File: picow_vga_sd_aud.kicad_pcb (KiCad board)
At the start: 2 copper layers, 74.4 x 53.1 mm, 98 parts, among them J1 10103594-0001LF, J10 Micro_SD_Card, J2 AudioJack3, J3 Micro_SD_Card, J4 L77HDE15SD1CH4F, J5 TSW-102-07-G-S, J6 Conn_01x18_Pin, J7 Conn_02x03_Odd_Even, SW1 SW_Push, SW2 SW_Push, SW3 SW_Push, SW4 SW_Push, SW5 SW_boot, U1 TLV70033_SOT23-5, U10 ER_OLEDM0.91_1x-I2C, U2 PicoW, U3 NC7WZ16P6X, U4 NCP1117ST33T3G, U5 W25Q128JVSIQ, U6 RP2040, U7 W25Q128JVSIQ, U8 TXS0108, U9 TXS0108, X1 12MHz

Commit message: Cambiar vias default de 0.8mm a 0.6mm de diámetro
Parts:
- moved R6 2.07 mm to (126.9, 63.1), turned to 0 degrees
- moved C25 0.15 mm to (124.8, 70.0)
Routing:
- net GND: track 515.5 -> 0.00 mm, vias 2 -> 0
- net /pico/QSPI_SS: track 145.6 -> 4.46 mm, vias 6 -> 0
- net /GPIO14: track 8.30 -> 23.7 mm
- net /GPIO13: track 21.2 -> 18.4 mm
- net +3V3: track 409.3 -> 411.6 mm
- net /GPIO12: track 24.8 -> 25.5 mm
- net /GPIO1: track 71.9 -> 72.5 mm

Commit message: Actualizar net classes y clearances del PCB
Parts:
- moved R6 20.3 mm to (128.8, 83.3), turned to 180 degrees
- moved C18 6.58 mm to (128.5, 82.3)
- moved C25 0.48 mm to (124.3, 70.0)
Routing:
- net /pico/QSPI_SD2: track 140.5 -> 0.00 mm, vias 6 -> 0
- net /GPIO14: track 23.7 -> 40.1 mm
- net /pico/QSPI_SS: track 4.46 -> 20.6 mm
- net /GPIO4: track 59.4 -> 46.6 mm, vias 3 -> 1
- net /GPIO3: track 38.8 -> 51.1 mm, vias 0 -> 1
- net /GPIO5: track 116.5 -> 110.9 mm
- net /GPIO1: track 72.5 -> 68.9 mm, vias 3 -> 1
- net /GPIO11: track 49.1 -> 46.0 mm
- net /GPIO8: track 40.2 -> 38.1 mm
- net /GPIO15: track 34.1 -> 34.8 mm

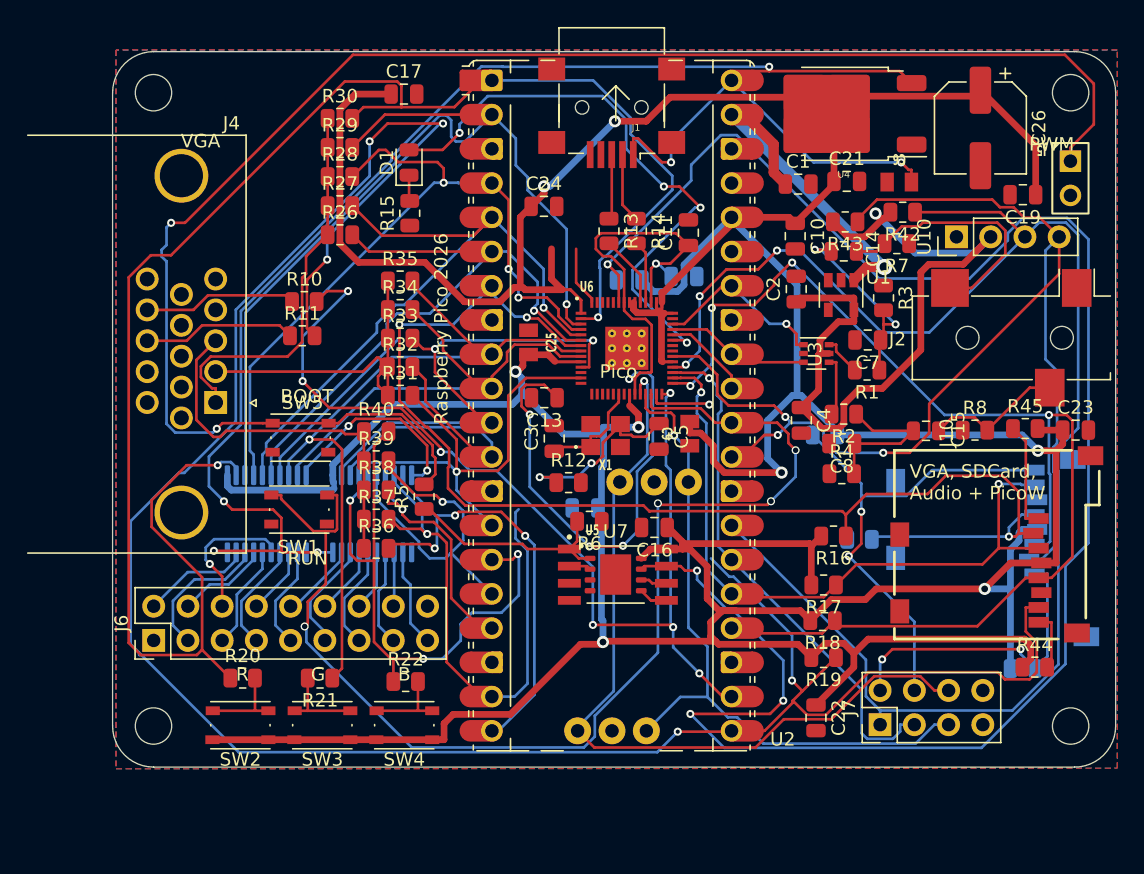
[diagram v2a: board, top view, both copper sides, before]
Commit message: Referencias Arial 0.8x0.8mm 0.12mm, horizontal y justify left en F.SilkS
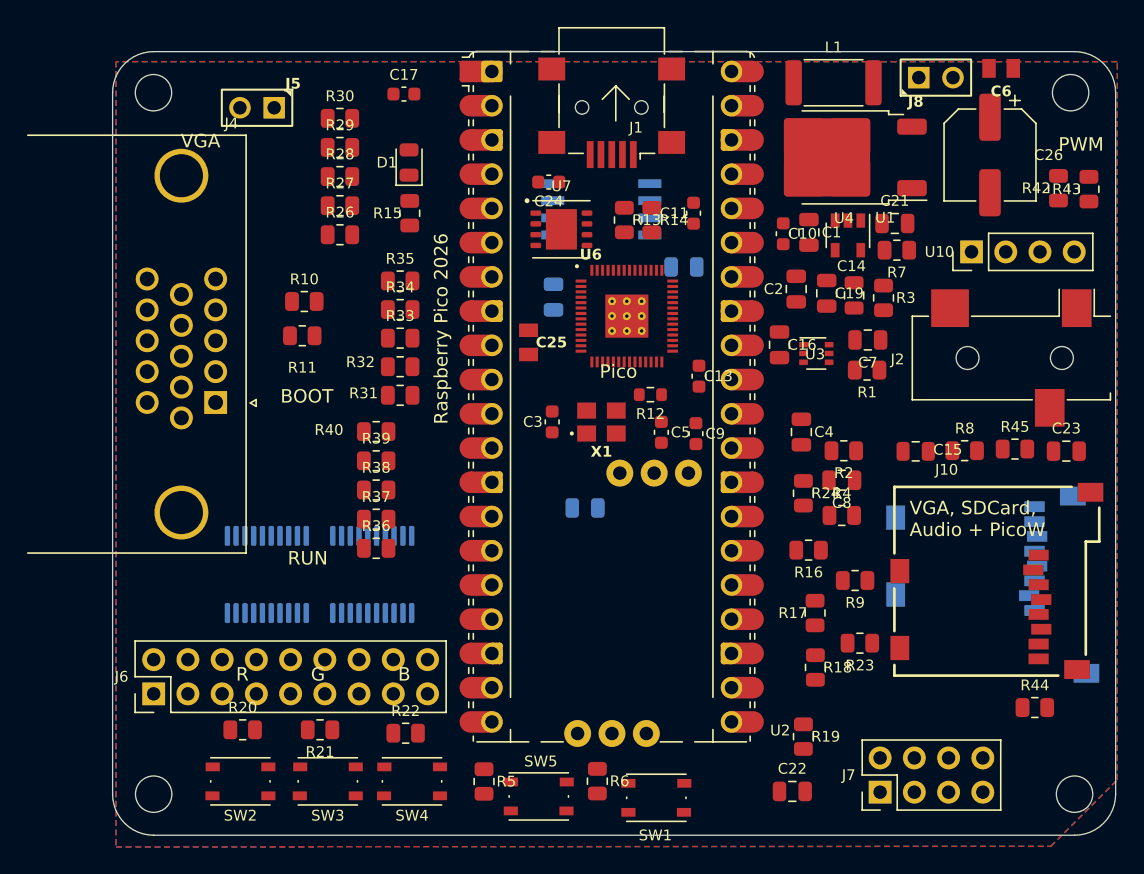
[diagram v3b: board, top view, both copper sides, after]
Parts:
- added J8: TSW-102-07-G-S, RaspberryPI PicoW:samtec_tsw-102-07-g-s, F.Cu at (154.6, 50.4)
- added L1: 100mH, Resistor_SMD:R_2512_6332Metric, F.Cu at (147.0, 50.8)
- C10, C11, C13, C17, C24, C3, C5: footprint Capacitor_SMD:C_0805_2012Metric -> Capacitor_SMD:C_0603_1608Metric
- C9: footprint RaspberryPI PicoW:generic_capc2012x125 -> Capacitor_SMD:C_0603_1608Metric
- R12: footprint Resistor_SMD:R_0805_2012Metric -> Resistor_SMD:R_0603_1608Metric
- R23, R24, R9: moved to F.Cu
- U5: moved to B.Cu
- moved J5 60.6 mm to (104.2, 52.6), turned to 180 degrees
- moved SW1 34.0 mm to (133.8, 103.8)
- moved SW5 32.0 mm to (125.1, 103.7)
- moved U5 27.1 mm to (129.7, 60.2), turned to 180 degrees
- moved U7 25.9 mm to (126.8, 61.6)
- moved R5 21.6 mm to (121.0, 102.6), turned to -90 degrees
- moved R6 19.3 mm to (129.4, 102.6), turned to -90 degrees
- moved R43 18.2 mm to (165.9, 58.7), turned to 90 degrees
- moved C16 16.4 mm to (142.9, 70.2), turned to -90 degrees
- moved C19 16.3 mm to (146.5, 66.4), turned to -90 degrees
- moved R23 12.2 mm to (148.9, 92.4)
- moved R42 11.7 mm to (163.6, 58.6), turned to 90 degrees
- moved C13 11.6 mm to (137.0, 72.5), turned to -90 degrees
- moved C6 11.3 mm to (159.4, 49.7), turned to 0 degrees
- moved R12 8.91 mm to (133.4, 73.9), turned to 180 degrees
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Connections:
- C2 pad 1: +3.3VA -> +3V3
- C4 pad 1: +3.3VA -> +3V3
- C6 pad 1: VBUS -> Net-(U4-IN)
- R42 pad 2: +3.3VA -> +3V3
- R43 pad 2: +3.3VA -> +3V3
- U1 pad 5: +3.3VA -> +3V3
- U10 pad 2: +3.3VA -> +3V3
- U3 pad 5: +3.3VA -> +3V3
- U4 pad 3: VBUS -> Net-(U4-IN)
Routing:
- net +3V3: track 411.5 -> 0.00 mm, vias 8 -> 0
- net /GPIO16: track 173.8 -> 0.00 mm, vias 6 -> 0
- net /pico/QSPI_SD3: track 138.7 -> 0.00 mm, vias 4 -> 0
- net /GPIO0: track 127.6 -> 0.00 mm, vias 2 -> 0
- net VBUS: track 123.6 -> 0.00 mm, vias 6 -> 0
- net /pico/~{USB_BOOT}: track 121.2 -> 0.00 mm, vias 2 -> 0
- net /GPIO21: track 118.6 -> 0.00 mm, vias 3 -> 0
- net /GPIO5: track 110.9 -> 0.00 mm, vias 3 -> 0
- net /GPIO22: track 91.1 -> 0.00 mm, vias 3 -> 0
- net /GPIO18: track 90.0 -> 0.00 mm, vias 4 -> 0
- net /RUN: track 89.1 -> 0.00 mm, vias 4 -> 0
- net /GPIO17: track 75.0 -> 0.00 mm, vias 7 -> 0
- net /GPIO1: track 68.9 -> 0.00 mm, vias 1 -> 0
- net +1V1: track 65.4 -> 0.00 mm, vias 5 -> 0
- net /SWCLK: track 59.9 -> 0.00 mm, vias 1 -> 0
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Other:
- board size 74.4 x 53.1 mm -> 74.4 x 58.1 mm
